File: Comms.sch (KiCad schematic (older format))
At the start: 47 parts, among them J1 Conn_01x05, J2 USB_B_Micro, U1 93LCxxB, U2 FT232H, U3 ADM2682E, U4 TPD2E2U06, U5 TPD2E2U06, Y1 12MHz

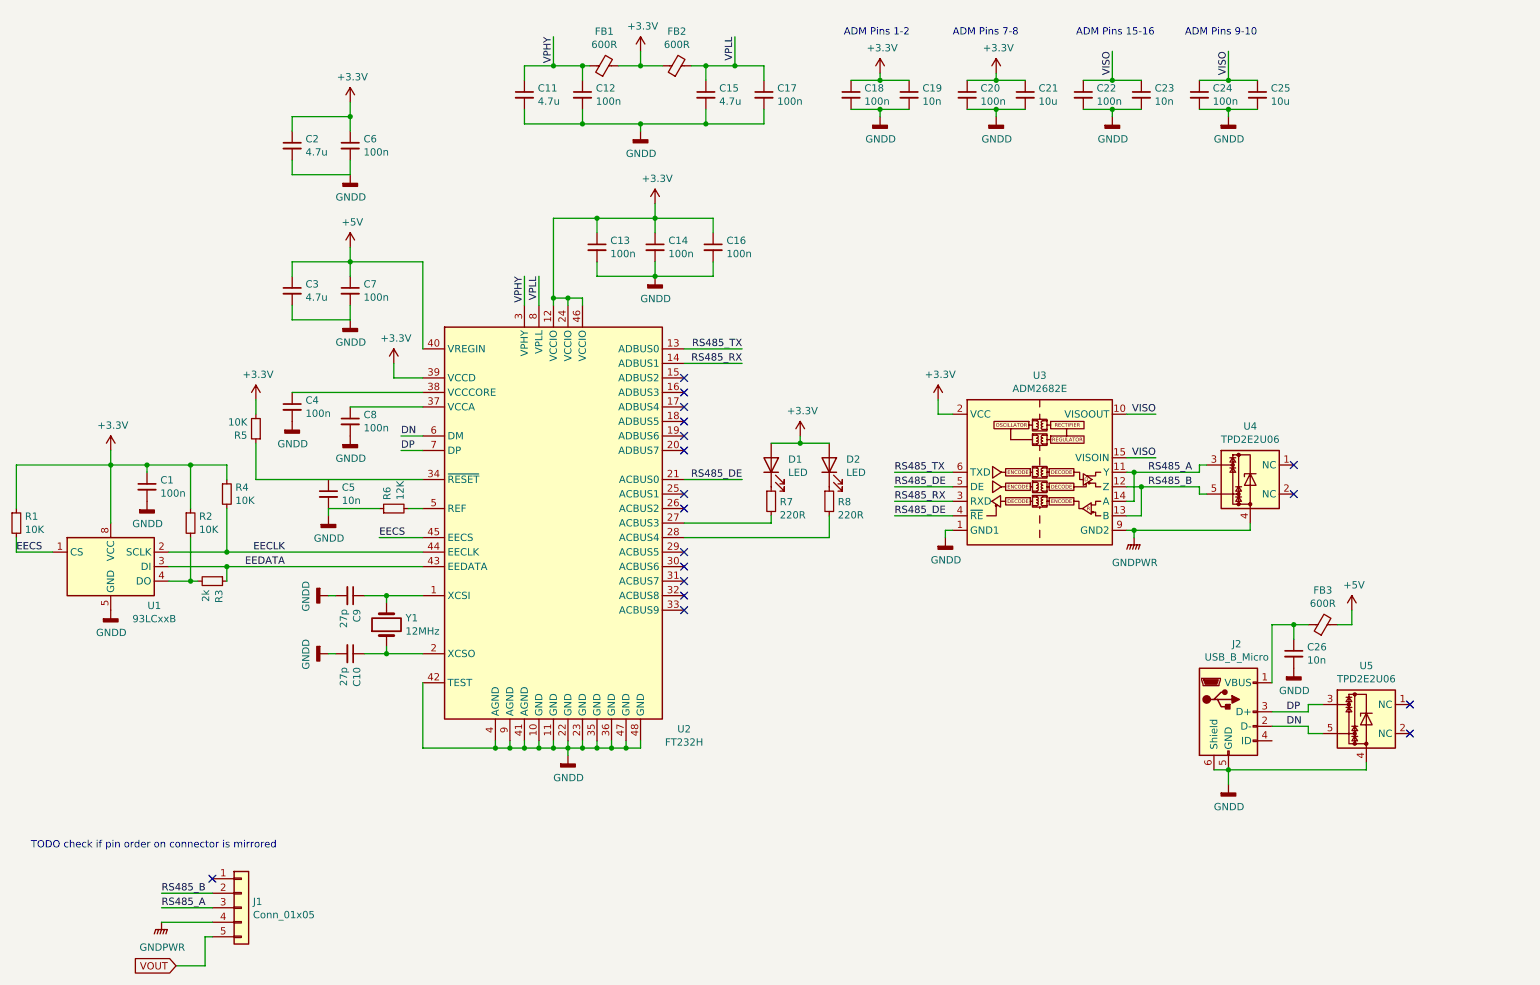
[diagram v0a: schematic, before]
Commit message: Added protection from motor regeneration through capacitors + MOSFET, started placement and routing
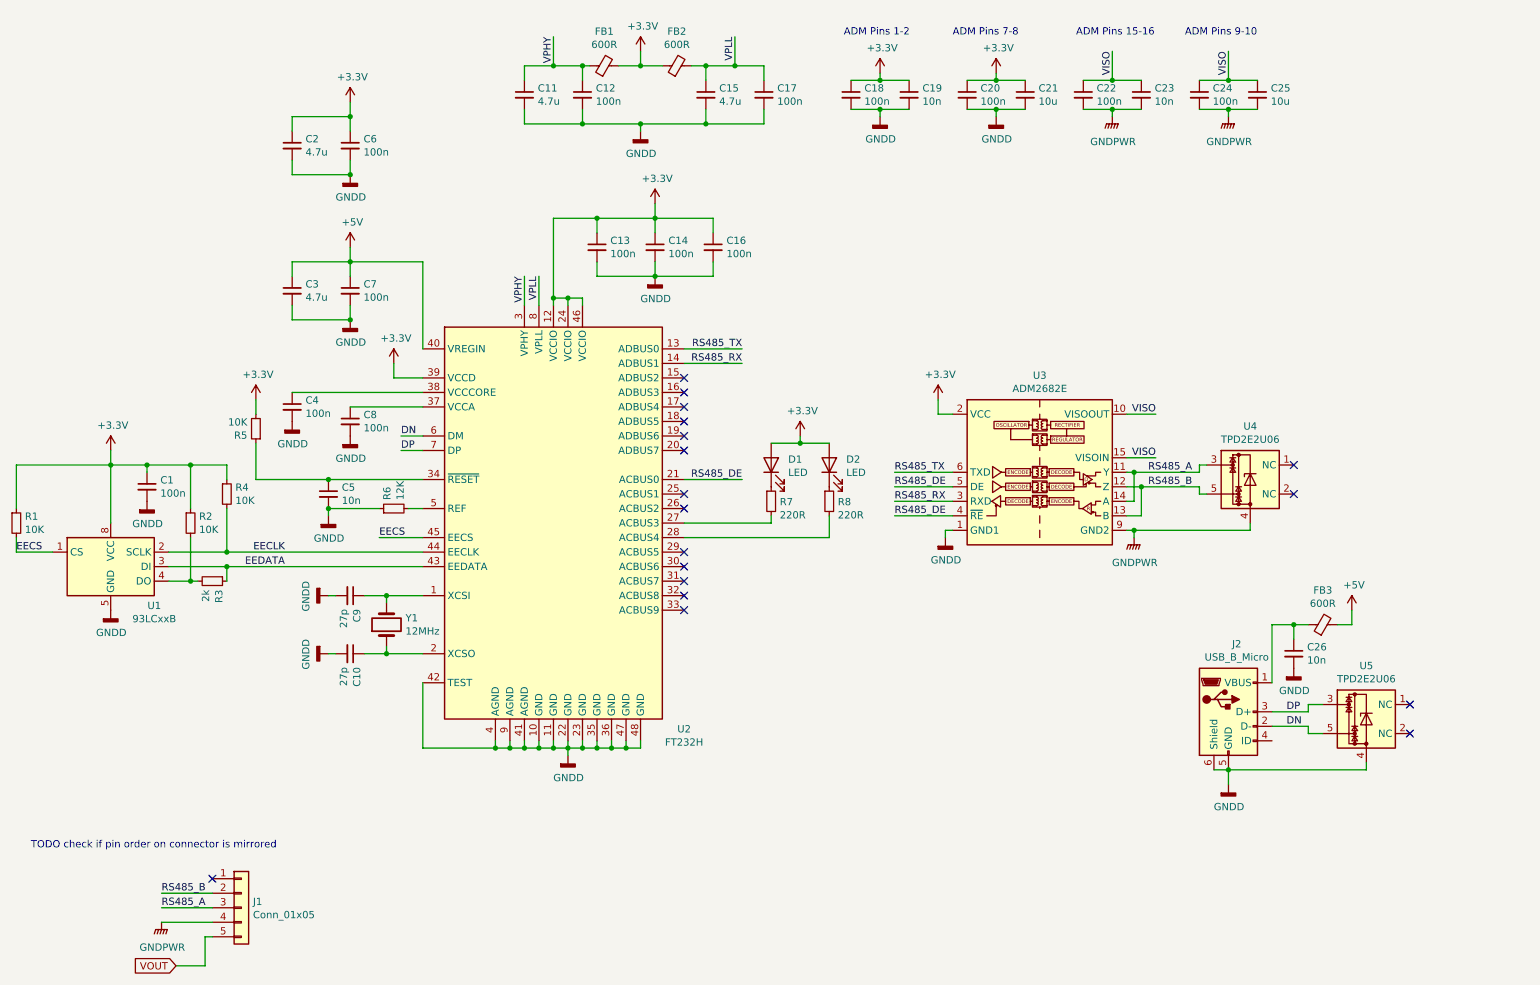
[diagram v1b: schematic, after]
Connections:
- net GNDD: no longer C22.2, C23.2, C24.2, C25.2
- net GNDPWR: now also C22.2, C23.2, C24.2, C25.2
- net at R5.1, U2.34 (~RESET): now also C5.1
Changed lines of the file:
@@
 EESchema Schematic File Version 5
-LIBS:blue_inputboard-cache
+LIBS:blue_interface_board-cache
 EELAYER 29 0
 EELAYER END
@@
 Wire Wire Line
 	8050 1150 8250 1150
-$Comp
-L power:GNDD #PWR0107
-U 1 1 5D293F1C
-P 9050 1400
-F 0 "#PWR0107" H 9050 1150 50  0001 C CNN
-F 1 "GNDD" H 9054 1245 50  0000 C CNN
-F 2 "" H 9050 1400 50  0001 C CNN
-F 3 "" H 9050 1400 50  0001 C CNN
-	1    9050 1400
-	1    0    0    -1
-$EndComp
 Connection ~ 6650 1150
 Text Label 9450 5600 0    50   ~ 0
@@
 Text Label 1700 6750 0    50   ~ 0
 RS485_B
-$Comp
-L power:GNDD #PWR0108
-U 1 1 5D293F19
-P 8250 1400
-F 0 "#PWR0108" H 8250 1150 50  0001 C CNN
-F 1 "GNDD" H 8254 1245 50  0000 C CNN
-F 2 "" H 8250 1400 50  0001 C CNN
-F 3 "" H 8250 1400 50  0001 C CNN
-	1    8250 1400
-	1    0    0    -1
-$EndComp
 Connection ~ 6650 1350
 $Comp
@@
 $EndComp
 Wire Wire Line
-	2350 3900 3500 3900
+	2350 3900 2850 3900
 Wire Wire Line
 	2150 3900 2150 3800
@@
 Wire Wire Line
 	2000 7250 2000 7050
+Connection ~ 3000 2800
+Connection ~ 3000 1800
+Connection ~ 2850 3900
+Wire Wire Line
+	2850 3900 3500 3900
+Connection ~ 2850 4100
+$Comp
+L power:GNDPWR #PWR?
+U 1 1 5D33261B
+P 8250 1400
+F 0 "#PWR?" H 8250 1150 50  0001 C CNN
+F 1 "GNDPWR" H 8255 1227 50  0000 C CNN
+F 2 "" H 8250 1400 50  0001 C CNN
+F 3 "" H 8250 1400 50  0001 C CNN
+	1    8250 1400
+	1    0    0    -1
+$EndComp
+$Comp
+L power:GNDPWR #PWR?
+U 1 1 5D332AC0
+P 9050 1400
+F 0 "#PWR?" H 9050 1150 50  0001 C CNN
+F 1 "GNDPWR" H 9055 1227 50  0000 C CNN
+F 2 "" H 9050 1400 50  0001 C CNN
+F 3 "" H 9050 1400 50  0001 C CNN
+	1    9050 1400
+	1    0    0    -1
+$EndComp
 $EndSCHEMATC

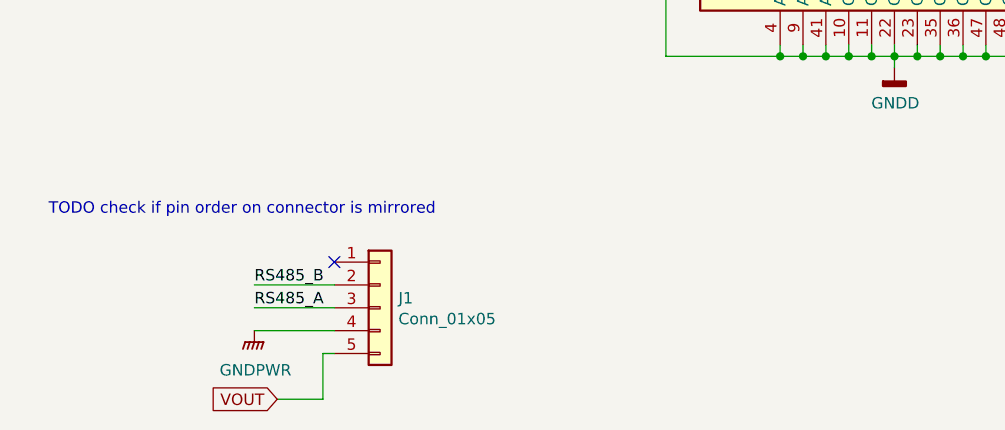
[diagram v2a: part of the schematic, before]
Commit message: Finished schematic, placement and routing, only silkscreen TODO
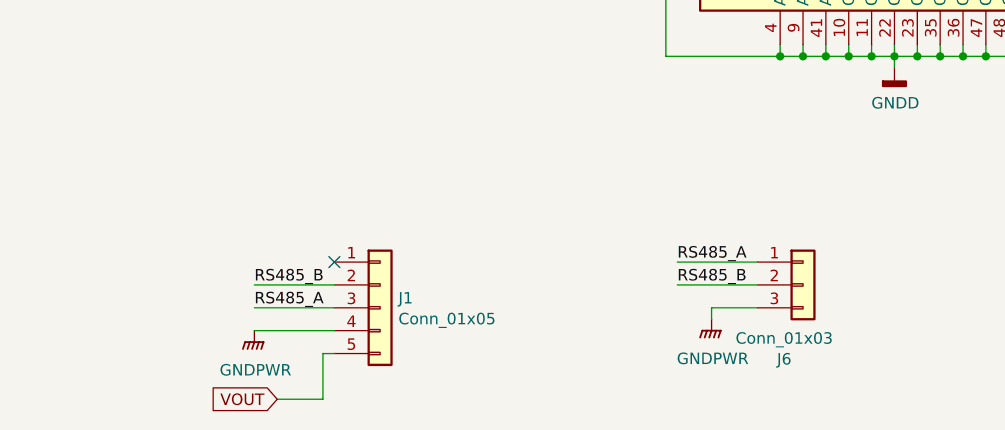
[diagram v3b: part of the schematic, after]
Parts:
- added J6: Conn_01x03, Connector_Molex:Molex_Nano-Fit_105313-xx03_1x03_P2.50mm_Horizontal, symbol Connector_Generic:Conn_01x03
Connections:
- net GNDPWR: now also J6.3 (Pin_3)
- net RS485_A: now also J6.1 (Pin_1)
- net RS485_B: now also J6.2 (Pin_2)
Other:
- note removed: "TODO check if pin order on connector is mirrored"
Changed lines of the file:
@@
 EESchema Schematic File Version 5
 LIBS:blue_interface_board-cache
-EELAYER 29 0
+EELAYER 30 0
 EELAYER END
 $Descr A4 11693 8268
@@
 	1    0    0    -1
 $EndComp
-Text Notes 800  6450 0    50   ~ 0
-TODO check if pin order on connector is mirrored
 Text Notes 8750 850  0    50   ~ 0
 ADM Pins 9-10
@@
 	1    0    0    -1
 $EndComp
+Wire Wire Line
+	3900 6650 3550 6650
+Text Label 3550 6650 0    50   ~ 0
+RS485_A
+Wire Wire Line
+	3550 6750 3900 6750
+$Comp
+L Connector_Generic:Conn_01x03 J6
+U 1 1 5D4BE1BB
+P 4100 6750
+F 0 "J6" H 4018 6425 50  0000 C CNN
+F 1 "Conn_01x03" H 4018 6516 50  0000 C CNN
+F 2 "Connector_Molex:Molex_Nano-Fit_105313-xx03_1x03_P2.50mm_Horizontal" H 4100 6750 50  0001 C CNN
+F 3 "~" H 4100 6750 50  0001 C CNN
+	1    4100 6750
+	1    0    0    -1
+$EndComp
+Text Label 3550 6750 0    50   ~ 0
+RS485_B
+$Comp
+L power:GNDPWR #PWR0157
+U 1 1 5D4DFA36
+P 3700 6900
+F 0 "#PWR0157" H 3700 6650 50  0001 C CNN
+F 1 "GNDPWR" H 3705 6727 50  0000 C CNN
+F 2 "" H 3700 6900 50  0001 C CNN
+F 3 "" H 3700 6900 50  0001 C CNN
+	1    3700 6900
+	1    0    0    -1
+$EndComp
+Wire Wire Line
+	3900 6850 3700 6850
+Wire Wire Line
+	3700 6850 3700 6900
 $EndSCHEMATC

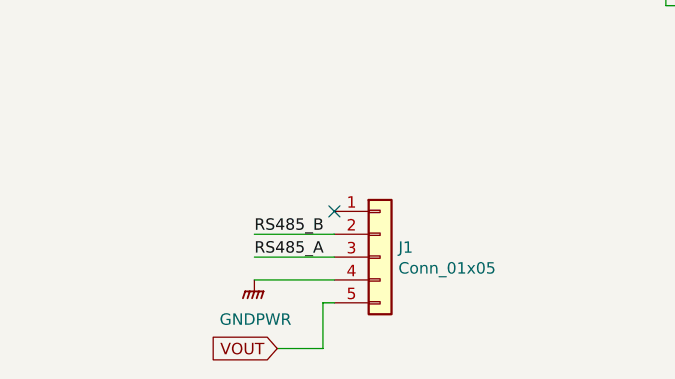
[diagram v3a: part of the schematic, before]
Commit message: Fixed flipped connector, changed most placement
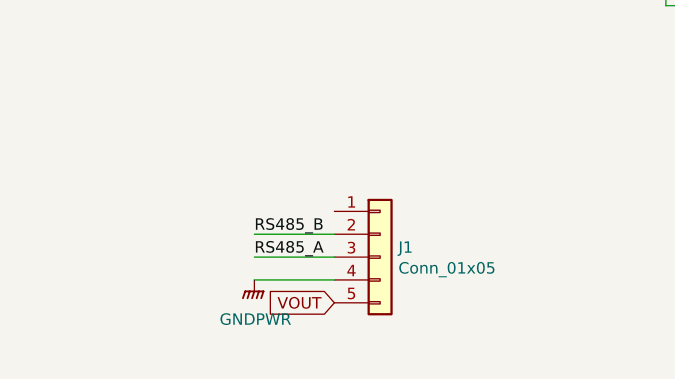
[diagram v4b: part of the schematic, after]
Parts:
- J1: footprint Connector_Molex:Molex_Micro-Fit_3.0_43650-0500_1x05_P3.00mm_Horizontal -> BLDC:molex-436500511
- J6: footprint Connector_Molex:Molex_Nano-Fit_105313-xx03_1x03_P2.50mm_Horizontal -> Connector_PinHeader_2.54mm:PinHeader_1x03_P2.54mm_Vertical
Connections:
- no-connect marks 18 -> 17
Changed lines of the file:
@@
 Comment3 ""
 Comment4 ""
+Comment5 ""
+Comment6 ""
+Comment7 ""
+Comment8 ""
+Comment9 ""
 $EndDescr
 Wire Wire Line
@@
 	6650 1150 6850 1150
 Wire Wire Line
-	2000 7050 2050 7050
-Wire Wire Line
 	1700 6750 2050 6750
 Wire Wire Line
 	2050 6850 1700 6850
-NoConn ~ 2050 6650
 Wire Wire Line
 	6650 1350 6450 1350
@@
 $EndComp
 Wire Wire Line
-	2050 6950 1700 6950
-Wire Wire Line
 	7450 1150 7450 1100
 Text Label 8250 950  3    50   ~ 0
@@
 	9350 5300 9350 4900
 $Comp
-L Connector_Generic:Conn_01x05 J1
-U 1 1 5D293F26
-P 2250 6850
-F 0 "J1" H 2330 6892 50  0000 L CNN
-F 1 "Conn_01x05" H 2330 6801 50  0000 L CNN
-F 2 "Connector_Molex:Molex_Micro-Fit_3.0_43650-0500_1x05_P3.00mm_Horizontal" H 2250 6850 50  0001 C CNN
-F 3 "~" H 2250 6850 50  0001 C CNN
-	1    2250 6850
-	1    0    0    -1
-$EndComp
-$Comp
 L Device:C_Small C22
 U 1 1 5D293F1A
@@
 Wire Wire Line
 	8850 1150 9050 1150
-Wire Wire Line
-	9050 5900 8950 5900
 Wire Wire Line
 	9500 5000 9500 4900
@@
 	1    0    0    -1
 $EndComp
-Text GLabel 1800 7250 0    50   Input ~ 0
+Text GLabel 2050 7050 0    50   Input ~ 0
 VOUT
-Wire Wire Line
-	1800 7250 2000 7250
-Wire Wire Line
-	2000 7250 2000 7050
 Connection ~ 3000 2800
 Connection ~ 3000 1800
@@
 F 0 "J6" H 4018 6425 50  0000 C CNN
 F 1 "Conn_01x03" H 4018 6516 50  0000 C CNN
-F 2 "Connector_Molex:Molex_Nano-Fit_105313-xx03_1x03_P2.50mm_Horizontal" H 4100 6750 50  0001 C CNN
+F 2 "Connector_PinHeader_2.54mm:PinHeader_1x03_P2.54mm_Vertical" H 4100 6750 50  0001 C CNN
 F 3 "~" H 4100 6750 50  0001 C CNN
 	1    4100 6750
@@
 Wire Wire Line
 	3700 6850 3700 6900
+$Comp
+L Connector_Generic:Conn_01x05 J1
+U 1 1 5D293F26
+P 2250 6850
+F 0 "J1" H 2330 6892 50  0000 L CNN
+F 1 "Conn_01x05" H 2330 6801 50  0000 L CNN
+F 2 "BLDC:molex-436500511" H 2250 6850 50  0001 C CNN
+F 3 "~" H 2250 6850 50  0001 C CNN
+	1    2250 6850
+	1    0    0    -1
+$EndComp
+Wire Wire Line
+	2050 6950 1700 6950
+Wire Wire Line
+	9050 5900 8950 5900
 $EndSCHEMATC

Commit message: Fix DRCs and minor improvements
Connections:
- net GNDD: now also J6.3 (Pin_3)
- net GNDPWR: no longer J6.3 (Pin_3)
- net RS485_A: no longer J6.1 (Pin_1)
- net RS485_B: no longer J6.2 (Pin_2)
- net RS485_RX: now also J6.2 (Pin_2)
- net RS485_TX: now also J6.1 (Pin_1)
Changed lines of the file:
@@
 EESchema Schematic File Version 5
-LIBS:blue_interface_board-cache
 EELAYER 30 0
 EELAYER END
@@
 Wire Wire Line
 	3900 6650 3550 6650
-Text Label 3550 6650 0    50   ~ 0
-RS485_A
 Wire Wire Line
 	3550 6750 3900 6750
@@
 	1    0    0    -1
 $EndComp
-Text Label 3550 6750 0    50   ~ 0
-RS485_B
-$Comp
-L power:GNDPWR #PWR0157
-U 1 1 5D4DFA36
-P 3700 6900
-F 0 "#PWR0157" H 3700 6650 50  0001 C CNN
-F 1 "GNDPWR" H 3705 6727 50  0000 C CNN
-F 2 "" H 3700 6900 50  0001 C CNN
-F 3 "" H 3700 6900 50  0001 C CNN
-	1    3700 6900
-	1    0    0    -1
-$EndComp
 Wire Wire Line
 	3900 6850 3700 6850
@@
 Wire Wire Line
 	9050 5900 8950 5900
+Text Label 3550 6650 0    50   ~ 0
+RS485_TX
+Text Label 3550 6750 0    50   ~ 0
+RS485_RX
+$Comp
+L power:GNDD #PWR0157
+U 1 1 5DD2A0BF
+P 3700 6900
+F 0 "#PWR0157" H 3700 6650 50  0001 C CNN
+F 1 "GNDD" H 3704 6745 50  0000 C CNN
+F 2 "" H 3700 6900 50  0001 C CNN
+F 3 "" H 3700 6900 50  0001 C CNN
+	1    3700 6900
+	1    0    0    -1
+$EndComp
 $EndSCHEMATC

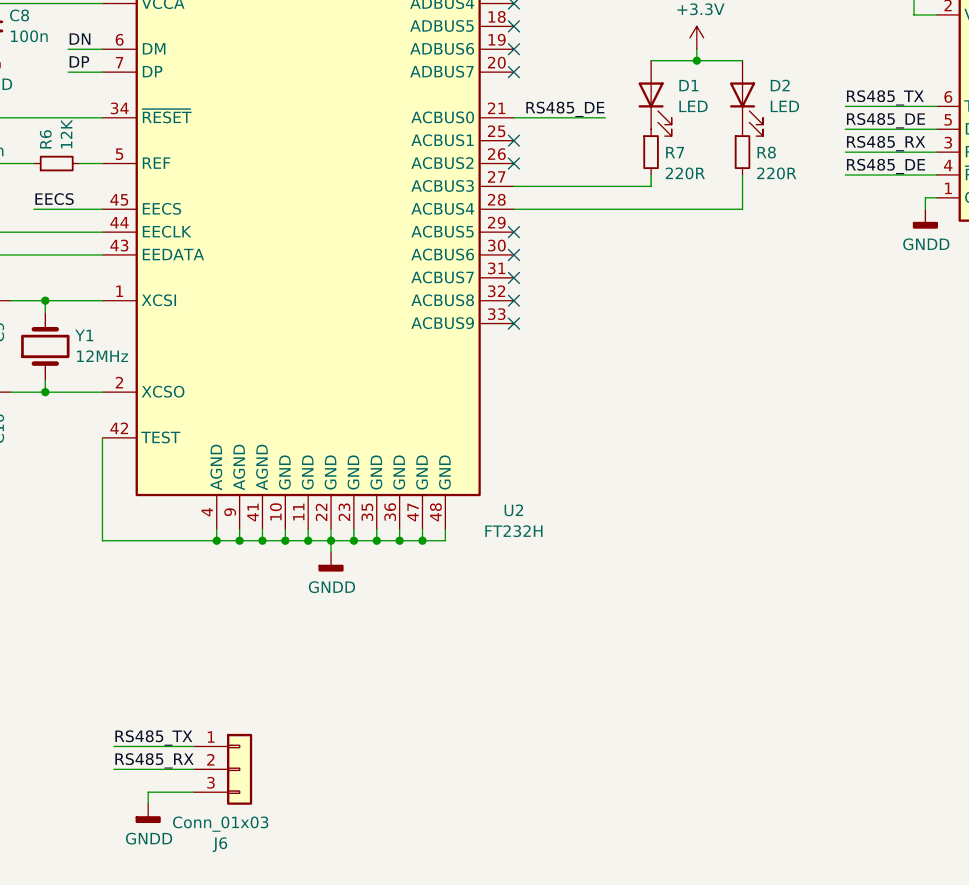
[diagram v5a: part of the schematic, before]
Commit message: Changed voltage regulator, added I2C interface
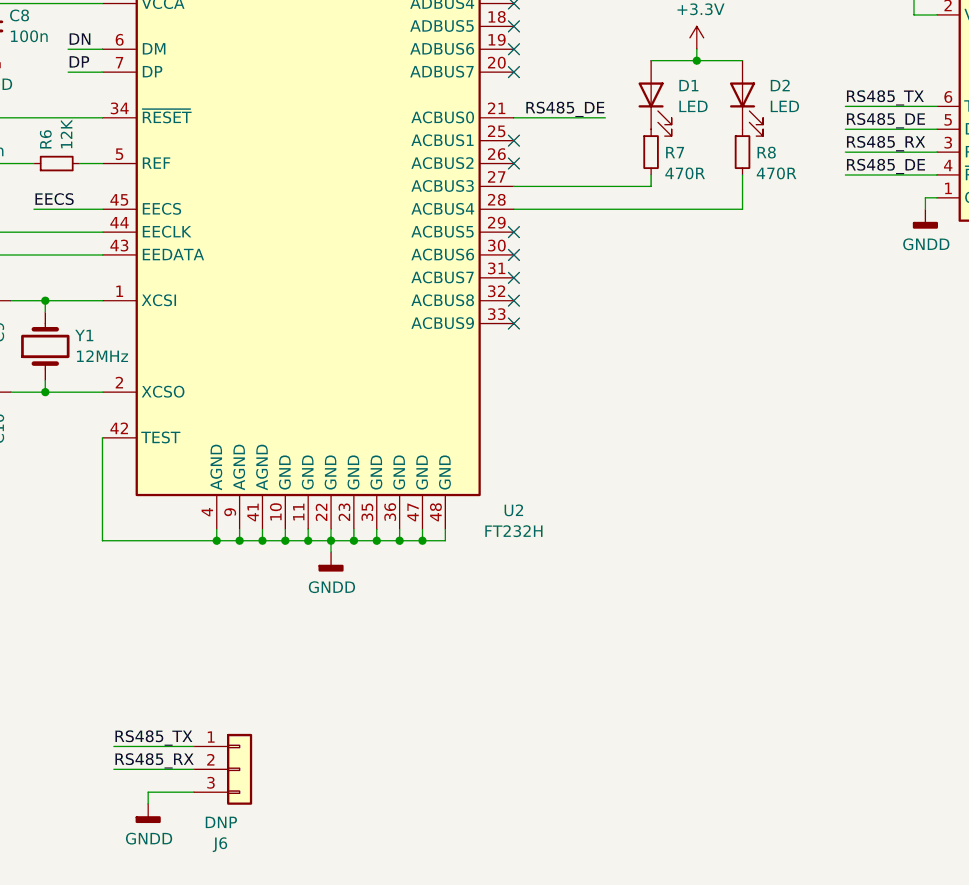
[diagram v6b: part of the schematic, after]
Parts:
- C1, C12, C13, C14, C16, C17, C18, C20, C22, C24, C4, C6, C7, C8: D1N (none) -> Digikey; D1PN (none) -> 1276-1258-1-ND; MFN (none) -> Samsung; MPN (none) -> CL10F104ZO8NNNC
- C10, C9: D1N (none) -> Digikey; D1PN (none) -> 311-1063-1-ND; MFN (none) -> Yageo; MPN (none) -> CC0603JRNPO9BN270
- C11, C15, C2, C3: D1N (none) -> Digikey; D1PN (none) -> 587-1441-1-ND; MFN (none) -> Tayio Yuden; MPN (none) -> LMK107BJ475KA-T
- C19, C23, C26, C5: D1N (none) -> Digikey; D1PN (none) -> 311-1572-1-ND; MFN (none) -> Yageo; MPN (none) -> CC0603KPX7R9BB103
- C21, C25: D1N (none) -> Digikey; D1PN (none) -> 490-14372-1-ND; MFN (none) -> Murata; MPN (none) -> GRM188R61A106KE69J
- D1, D2: D1N (none) -> Digikey; D1PN (none) -> 732-4980-1-ND; MFN (none) -> Wurth; MPN (none) -> 150060VS75000
- FB1, FB2, FB3: D1N (none) -> Digikey; D1PN (none) -> 732-1593-1-ND; MFN (none) -> Wurth; MPN (none) -> 742792651
- J1: D1N (none) -> Digikey; D1PN (none) -> 0436500511-ND; MFN (none) -> Molex; MPN (none) -> 436500511
- J2: D1N (none) -> Digikey; D1PN (none) -> 732-5960-6-ND; MFN (none) -> Wurth; MPN (none) -> 629105150521
- J6: value Conn_01x03 -> DNP; D1N (none) -> DNP; D1PN (none) -> DNP; MFN (none) -> DNP; MPN (none) -> DNP
- R1, R2, R4, R5: D1N (none) -> Digikey; D1PN (none) -> 311-10KGRCT-ND; MFN (none) -> Yageo; MPN (none) -> RC0603JR-0710KL
- R3: D1N (none) -> Digikey; D1PN (none) -> P2.0KDBCT-ND; MFN (none) -> Panasonic; MPN (none) -> ERA-3AEB202V
- R6: D1N (none) -> Digikey; D1PN (none) -> P12KDBCT-ND; MFN (none) -> Panasonic; MPN (none) -> ERA-3AEB123V
- R7, R8: value 220R -> 470R; D1N (none) -> Digikey; D1PN (none) -> A130089CT-ND; MFN (none) -> TE Connectivity; MPN (none) -> CRGCQ0603J470R
- U1: D1N (none) -> Digikey; D1PN (none) -> 93LC56B/SN-ND; MFN (none) -> Microchip; MPN (none) -> 93LC56B/SN
- U2: D1N (none) -> Digikey; D1PN (none) -> 768-1101-1-ND; MFN (none) -> FTDI; MPN (none) -> FT232HL-REEL
- U3: D1N (none) -> Digikey; D1PN (none) -> ADM2682EBRIZ-RL7CT-ND; MFN (none) -> Analog Devices; MPN (none) -> ADM2682EBRIZ-RL7
- U4, U5: D1N (none) -> Digikey; D1PN (none) -> 296-38361-1-ND; MFN (none) -> TI; MPN (none) -> TPD2E2U06DRLR
- Y1: D1N (none) -> Digikey; D1PN (none) -> 1253-1375-1-ND; MFN (none) -> Kyocera; MPN (none) -> CX5032GB12000H0HPQZ1
